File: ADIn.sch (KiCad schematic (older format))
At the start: 41 parts

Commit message: add RS422, RS232 filters
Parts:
- C? (x8): symbol ar2iss:C -> AR2ISS:C
- R? (x24): symbol ar2iss:R -> AR2ISS:R
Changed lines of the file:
@@
 $Descr A4 11693 8268
 encoding utf-8
-Sheet 4 7
+Sheet 4 10
 Title ""
 Date ""
@@
 $EndDescr
 $Comp
-L ar2iss:R R?
+L AR2ISS:R R?
 U 1 1 6069F1AD
 P 4200 1350
@@
 $EndComp
 $Comp
-L ar2iss:C C?
+L AR2ISS:C C?
 U 1 1 606A0627
 P 4500 1600
@@
 $EndComp
 $Comp
-L ar2iss:R R?
+L AR2ISS:R R?
 U 1 1 606A28F7
 P 5350 1600
@@
 $EndComp
 $Comp
-L ar2iss:R R?
+L AR2ISS:R R?
 U 1 1 606A2E2D
 P 5650 1350
@@
 $EndComp
 $Comp
-L ar2iss:R R?
+L AR2ISS:R R?
 U 1 1 606AAA50
 P 4200 2400
@@
 $EndComp
 $Comp
-L ar2iss:C C?
+L AR2ISS:C C?
 U 1 1 606AAA56
 P 4500 2650
@@
 $EndComp
 $Comp
-L ar2iss:R R?
+L AR2ISS:R R?
 U 1 1 606AAA62
 P 5350 2650
@@
 $EndComp
 $Comp
-L ar2iss:R R?
+L AR2ISS:R R?
 U 1 1 606AAA68
 P 5650 2400
@@
 	5350 2800 5350 2900
 $Comp
-L ar2iss:R R?
+L AR2ISS:R R?
 U 1 1 606AEF1D
 P 4200 3500
@@
 $EndComp
 $Comp
-L ar2iss:C C?
+L AR2ISS:C C?
 U 1 1 606AEF23
 P 4500 3750
@@
 $EndComp
 $Comp
-L ar2iss:R R?
+L AR2ISS:R R?
 U 1 1 606AEF2F
 P 5350 3750
@@
 $EndComp
 $Comp
-L ar2iss:R R?
+L AR2ISS:R R?
 U 1 1 606AEF35
 P 5650 3500
@@
 	5350 3900 5350 4000
 $Comp
-L ar2iss:R R?
+L AR2ISS:R R?
 U 1 1 606AEF5B
 P 4200 4700
@@
 $EndComp
 $Comp
-L ar2iss:C C?
+L AR2ISS:C C?
 U 1 1 606AEF61
 P 4500 4950
@@
 $EndComp
 $Comp
-L ar2iss:R R?
+L AR2ISS:R R?
 U 1 1 606AEF6D
 P 5350 4950
@@
 $EndComp
 $Comp
-L ar2iss:R R?
+L AR2ISS:R R?
 U 1 1 606AEF73
 P 5650 4700
@@
 	5350 5100 5350 5200
 $Comp
-L ar2iss:R R?
+L AR2ISS:R R?
 U 1 1 606C2FCD
 P 8300 1350
@@
 $EndComp
 $Comp
-L ar2iss:C C?
+L AR2ISS:C C?
 U 1 1 606C2FD3
 P 8600 1600
@@
 $EndComp
 $Comp
-L ar2iss:R R?
+L AR2ISS:R R?
 U 1 1 606C2FDF
 P 9450 1600
@@
 $EndComp
 $Comp
-L ar2iss:R R?
+L AR2ISS:R R?
 U 1 1 606C2FE5
 P 9750 1350
@@
 	9450 1750 9450 1850
 $Comp
-L ar2iss:R R?
+L AR2ISS:R R?
 U 1 1 606C300B
 P 8300 2500
@@
 $EndComp
 $Comp
-L ar2iss:C C?
+L AR2ISS:C C?
 U 1 1 606C3011
 P 8600 2750
@@
 $EndComp
 $Comp
-L ar2iss:R R?
+L AR2ISS:R R?
 U 1 1 606C301D
 P 9450 2750
@@
 $EndComp
 $Comp
-L ar2iss:R R?
+L AR2ISS:R R?
 U 1 1 606C3023
 P 9750 2500
@@
 	9450 2900 9450 3000
 $Comp
-L ar2iss:R R?
+L AR2ISS:R R?
 U 1 1 606C3049
 P 8300 3700
@@
 $EndComp
 $Comp
-L ar2iss:C C?
+L AR2ISS:C C?
 U 1 1 606C304F
 P 8600 3950
@@
 $EndComp
 $Comp
-L ar2iss:R R?
+L AR2ISS:R R?
 U 1 1 606C305B
 P 9450 3950
@@
 $EndComp
 $Comp
-L ar2iss:R R?
+L AR2ISS:R R?
 U 1 1 606C3061
 P 9750 3700
@@
 	9450 4100 9450 4200
 $Comp
-L ar2iss:R R?
+L AR2ISS:R R?
 U 1 1 606C3087
 P 8300 4850
@@
 $EndComp
 $Comp
-L ar2iss:C C?
+L AR2ISS:C C?
 U 1 1 606C308D
 P 8600 5100
@@
 $EndComp
 $Comp
-L ar2iss:R R?
+L AR2ISS:R R?
 U 1 1 606C3099
 P 9450 5100
@@
 $EndComp
 $Comp
-L ar2iss:R R?
+L AR2ISS:R R?
 U 1 1 606C309F
 P 9750 4850
@@
 NoConn ~ 6300 5950
 NoConn ~ 10400 5950
+Text HLabel 5500 900  0    50   Input ~ 0
+DA_IN_LL
 Wire Bus Line
 	10400 900  10400 5950
 Wire Bus Line
 	6300 900  6300 5950
-Text HLabel 5500 900  0    50   Input ~ 0
-DA_IN_LL
 $EndSCHEMATC

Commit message: start placement
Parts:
- C1, C2, C3, C4, C5, C6, C7, C8: renamed from C?; footprint (none) -> Capacitor_SMD:C_0603_1608Metric
- D10, D11, D12, D13, D14, D15, D16, D9: renamed from D?; value 3,6V -> MMSZ3V6CW; footprint (none) -> Diode_SMD:D_SOD-123
- J5: renamed from J?; footprint (none) -> AR2ISS:250-208
- R12, R13, R14, R15, R16, R17, R18, R19, R20, R21, R22, R23, R24, R25, R26, R27, R28, R29, R30, R31, R32, R33, R34, R35: renamed from R?; footprint (none) -> Resistor_SMD:R_0603_1608Metric
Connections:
- no-connect marks 2 -> 0

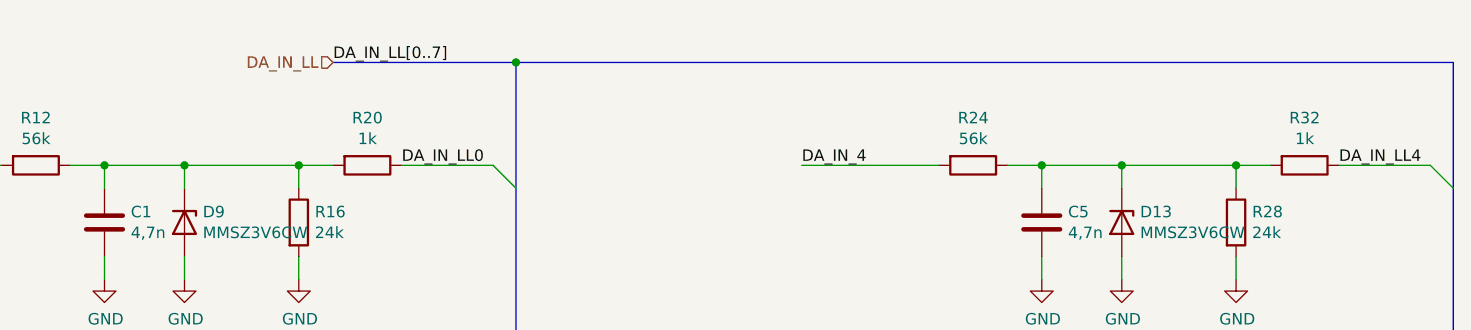
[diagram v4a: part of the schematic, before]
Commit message: add TLE5602
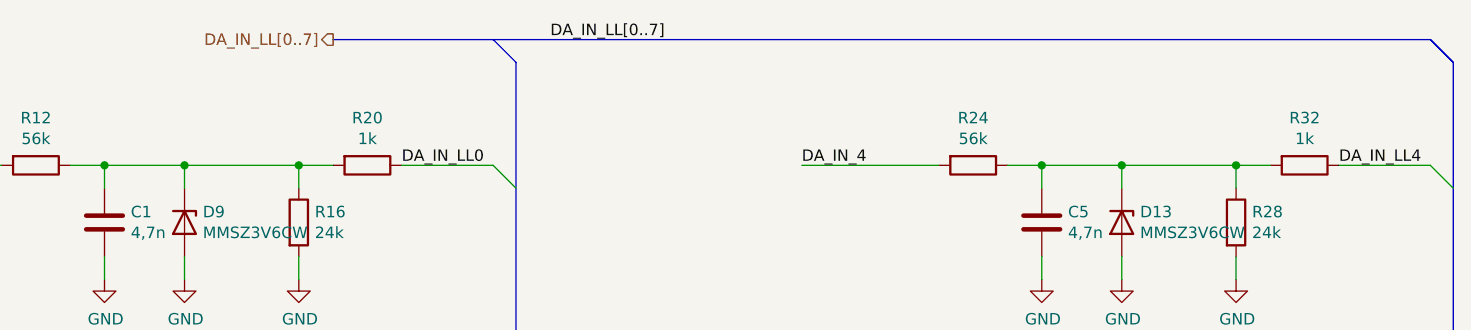
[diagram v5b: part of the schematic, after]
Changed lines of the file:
@@
 $Descr A4 11693 8268
 encoding utf-8
-Sheet 3 22
+Sheet 22 22
 Title ""
 Date ""
@@
 	8150 3700 7550 3700
 Entry Wire Line
-	6200 1350 6300 1450
-Entry Wire Line
 	6200 2400 6300 2500
 Entry Wire Line
@@
 Entry Wire Line
 	10300 4850 10400 4950
-Text Label 5500 900  0    50   ~ 0
+Text Label 6450 800  0    50   ~ 0
 DA_IN_LL[0..7]
 Text Label 5800 1350 0    50   ~ 0
@@
 Wire Wire Line
 	9900 1350 10300 1350
+Text HLabel 5500 800  0    50   Output ~ 0
+DA_IN_LL[0..7]
+Entry Wire Line
+	6200 1350 6300 1450
+Entry Bus Bus
+	10300 800  10400 900
+Entry Bus Bus
+	6200 800  6300 900
+Entry Bus Bus
+	10300 800  10400 900
+Entry Bus Bus
+	10300 800  10400 900
 Wire Bus Line
-	6300 900  5500 900
-Wire Bus Line
-	10400 900  6300 900
-Connection ~ 6300 900
-Text HLabel 5500 900  0    50   Input ~ 0
-DA_IN_LL
+	5500 800  10300 800
 Wire Bus Line
 	10400 900  10400 4950
